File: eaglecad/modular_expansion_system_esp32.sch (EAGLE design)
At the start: 34 parts, among them IC1 74LS30N, IC10 74LS244N, IC2 74LS04N, IC3 74LS04N, IC4 74LS00N, IC5 74LS04N, IC6 74LS74N, IC7 74LS00N, IC9 74S373N, J1 J1_ADDRESS_CON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

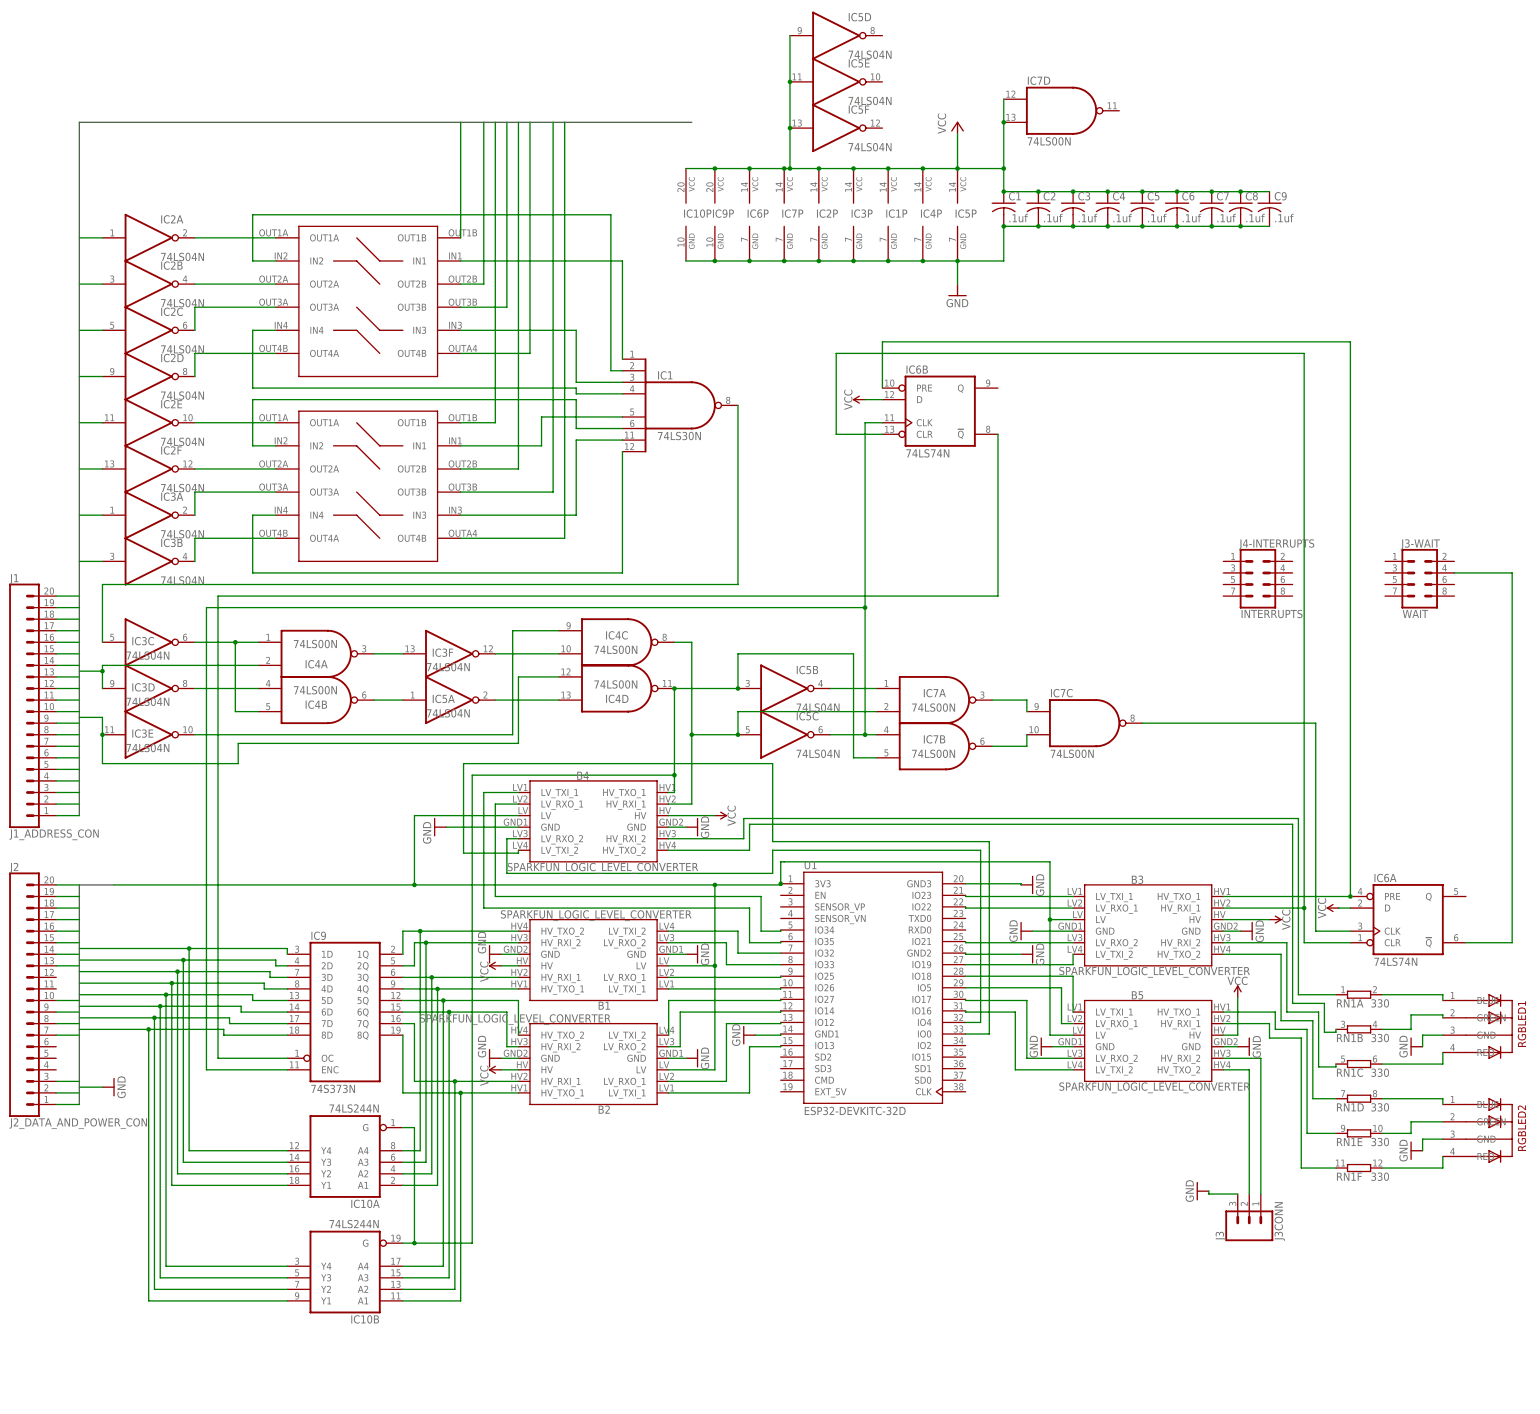
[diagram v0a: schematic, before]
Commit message: first 'working' ESP32 code and board design
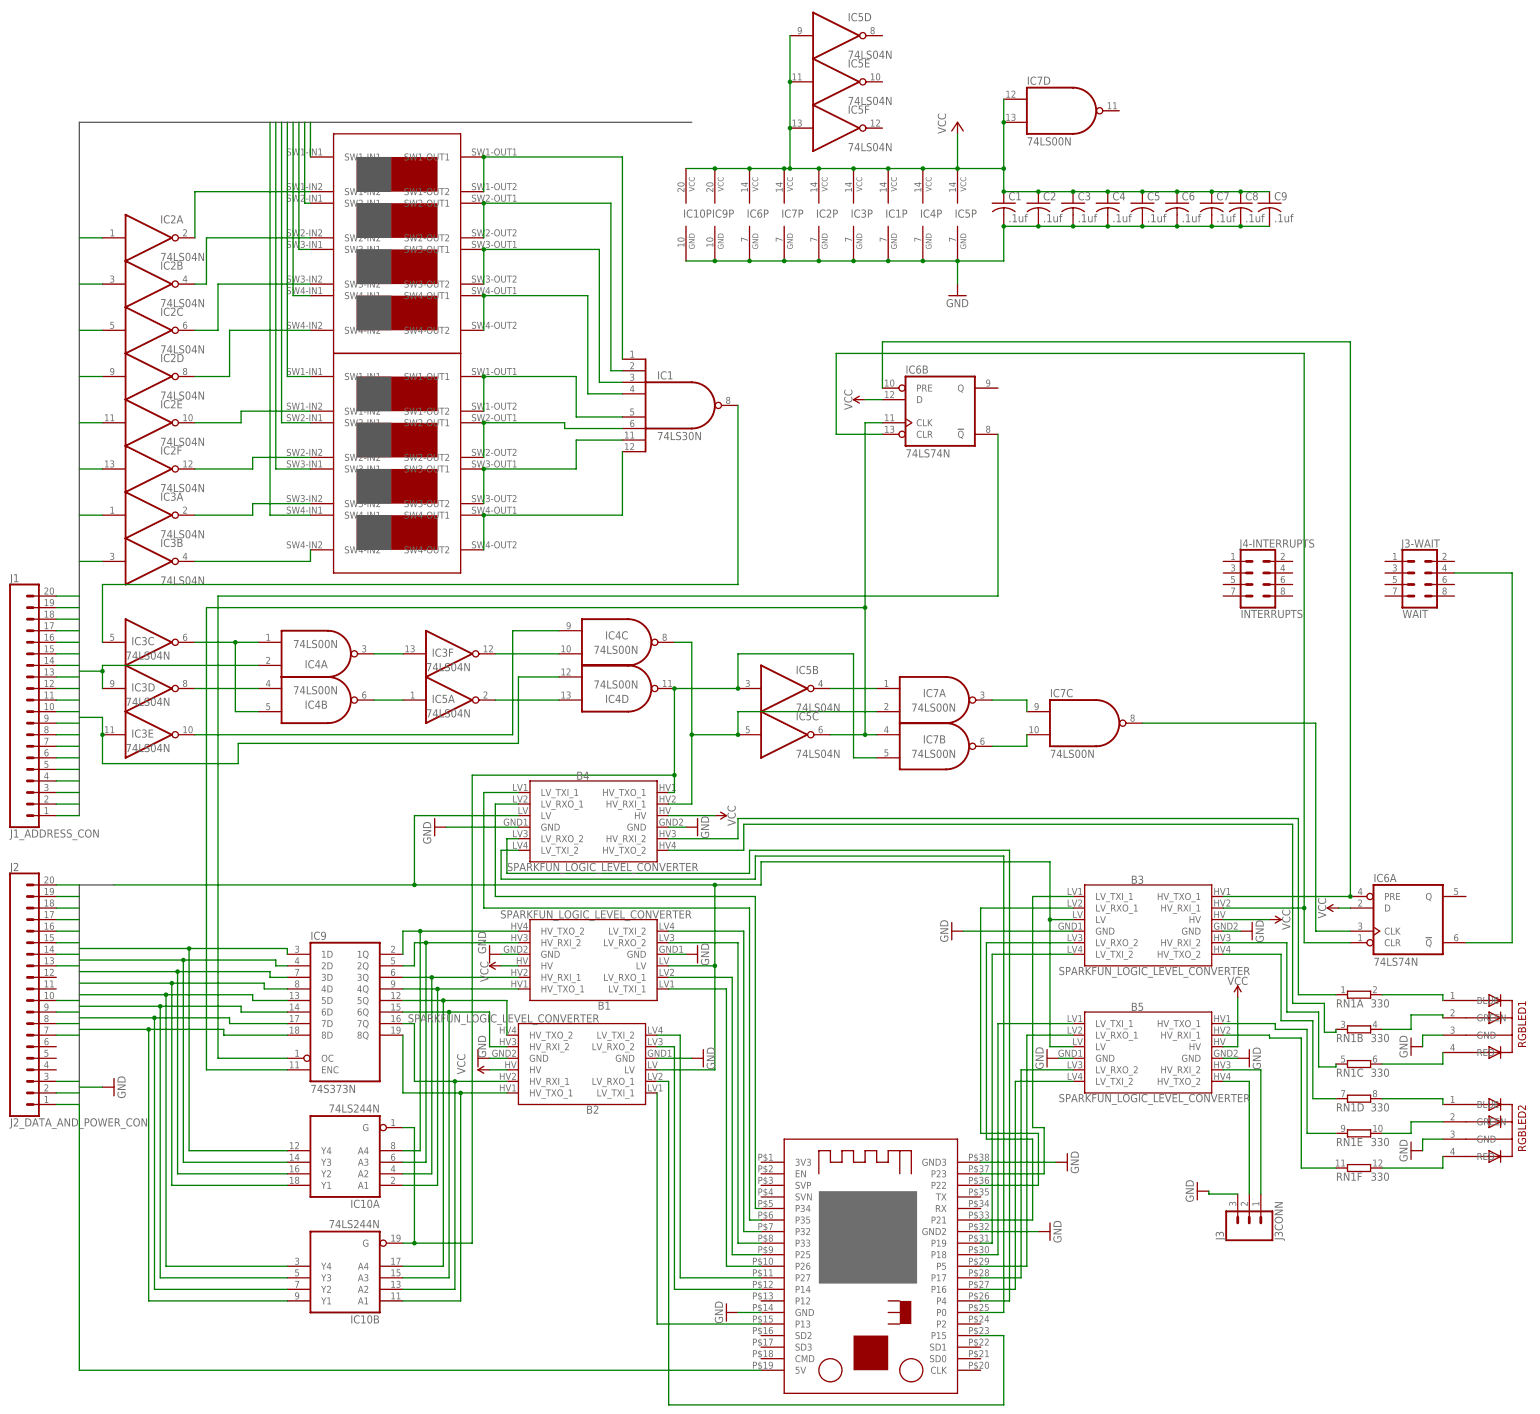
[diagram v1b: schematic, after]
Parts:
- removed U1: ESP32-DEVKITC-32D, ESP32-DEVKITC-32D:ESP32-DEVKITC-32D
- added U$1: ESP32S, TMS99:ESP32S
- SW1, SW2: value 76SC04T -> CTS206-124; device TMS99:76SC04T -> TMS99:CTS206-124
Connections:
- net N$17 renamed IC6_PRE_HV
- net N$18 renamed IC6_CLR_HV
- net N$27 renamed RGBLED1_B_5V
- net N$28 renamed RGBLED1_G_5V
- net N$29 renamed RGBLED1_R_5V
- net N$30 renamed RGBLED2_B_5V
- net N$31 renamed RGBLED2_G_5V
- net N$32 renamed RGBLED1_B
- net N$33 renamed RGBLED2_R_5V
- net N$34 renamed RGBLED1_G
- net N$35 renamed RGBLED1_R
- net N$36 renamed RGBLED2_B
- net N$37 renamed RGBLED2_G
- net N$38 renamed RGBLED2_R
- removed net N$1: IC1A.I0, SW1.IN1
- removed net N$10: B3.LV_RXO_1, U1.IO22
- removed net N$11: B3.LV_RXO_2, U1.IO21
- removed net N$16: B3.LV_TXI_2, U1.IO19
- removed net N$19: B5.LV_TXI_1, U1.IO18
- removed net N$2: IC1A.I1, SW1.IN2
- removed net N$22: B5.LV_RXO_1, U1.IO5
- removed net N$25: B4.LV_RXO_2, U1.IO4
- removed net N$26: B4.LV_TXI_2, U1.IO0
- removed net N$3: B3.LV_TXI_1, U1.IO23
- removed net N$4: IC1A.I2, SW1.IN3
- removed net N$5: IC1A.I3, SW1.IN4
- removed net N$6: IC1A.I4, SW2.IN1
- removed net N$7: IC1A.I5, SW2.IN2
- removed net N$8: IC1A.I6, SW2.IN3
- removed net N$9: IC1A.I7, SW2.IN4
- new net A0_OR_NOT_A0: IC1A.I7, SW1.SW4-OUT1, SW1.SW4-OUT2
- new net A1_OR_NOT_A1: IC1A.I6, SW1.SW3-OUT1, SW1.SW3-OUT2
- new net A2_OR_NOT_A2: IC1A.I5, SW1.SW2-OUT1, SW1.SW2-OUT2
- new net A3_OR_NOT_A3: IC1A.I4, SW1.SW1-OUT1, SW1.SW1-OUT2
- new net A4_OR_NOT_A4: IC1A.I3, SW2.SW4-OUT1, SW2.SW4-OUT2
- new net A5_OR_NOT_A5: IC1A.I2, SW2.SW3-OUT1, SW2.SW3-OUT2
- new net A6_OR_NOT_A6: IC1A.I1, SW2.SW2-OUT1, SW2.SW2-OUT2
- new net A7_OR_NOT_A7: IC1A.I0, SW2.SW1-OUT1, SW2.SW1-OUT2
- new net IC6A_CLR_LV: B3.LV_RXO_1, U$1.P22
- new net IC6A_PRE_LV: B3.LV_TXI_1, U$1.P23
- new net RGBLED1_B_LV: B4.LV_RXO_2, U$1.P4
- new net RGBLED1_G_LV: B4.LV_TXI_2, U$1.P0
- new net RGBLED1_R_LV: B3.LV_RXO_2, U$1.P21
- new net RGBLED2_B_LV: B3.LV_TXI_2, U$1.P19
- new net RGBLED2_G_LV: B5.LV_TXI_1, U$1.P18
- new net RGBLED2_R_LV: B5.LV_RXO_1, U$1.P5
- net A0: now also SW1.SW4-IN1; no longer SW2.OUT4B
- net A1: now also SW1.SW3-IN1; no longer SW2.OUT3B
- net A2: now also SW1.SW2-IN1; no longer SW2.OUT2B
- net A3: now also SW1.SW1-IN1; no longer SW2.OUT1B
- net A4: now also SW2.SW4-IN1; no longer SW1.OUT4B
- net A5: now also SW2.SW3-IN1; no longer SW1.OUT3B
- net A6: now also SW2.SW2-IN1; no longer SW1.OUT2B
- net A7: now also SW2.SW1-IN1; no longer SW1.OUT1B
- net D0_LV: now also U$1.P13; no longer U1.IO13
- net D1_LV: now also U$1.P15; no longer U1.IO12
- net D2_LV: now also U$1.P14; no longer U1.IO14
- net D3_LV: now also U$1.P27; no longer U1.IO27
- net D4_LV: now also U$1.P26; no longer U1.IO26
- net D5_LV: now also U$1.P25; no longer U1.IO25
- net D6_LV: now also U$1.P33; no longer U1.IO33
- net D7_LV: now also U$1.P32; no longer U1.IO32
- net GND: now also U$1.GND, U$1.GND2, U$1.GND3; no longer U1.GND1, U1.GND2, U1.GND3
- net N$23: now also U$1.P17; no longer U1.IO17
- net N$24: now also U$1.P16; no longer U1.IO16
- net NOT_A0: now also SW1.SW4-IN2; no longer SW2.OUT4A
- net NOT_A1: now also SW1.SW3-IN2; no longer SW2.OUT3A
- net NOT_A2: now also SW1.SW2-IN2; no longer SW2.OUT2A
- net NOT_A3: now also SW1.SW1-IN2; no longer SW2.OUT1A
- net NOT_A4: now also SW2.SW4-IN2; no longer SW1.OUT4A
- net NOT_A5: now also SW2.SW3-IN2; no longer SW1.OUT3A
- net NOT_A6: now also SW2.SW2-IN2; no longer SW1.OUT2A
- net NOT_A7: now also SW2.SW1-IN2; no longer SW1.OUT1A
- net VCC: now also U$1.5V
- net VCC/2: no longer U1.3V3
- net WIFI_IN_LV_: now also U$1.P35; no longer U1.IO35
- net WIFI_OUT_LV_: now also U$1.P34; no longer U1.IO34
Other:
- moved on the sheet: B2, B5
